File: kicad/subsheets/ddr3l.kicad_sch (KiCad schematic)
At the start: 1 part, among them U5 MT41K256M16TW-107:P

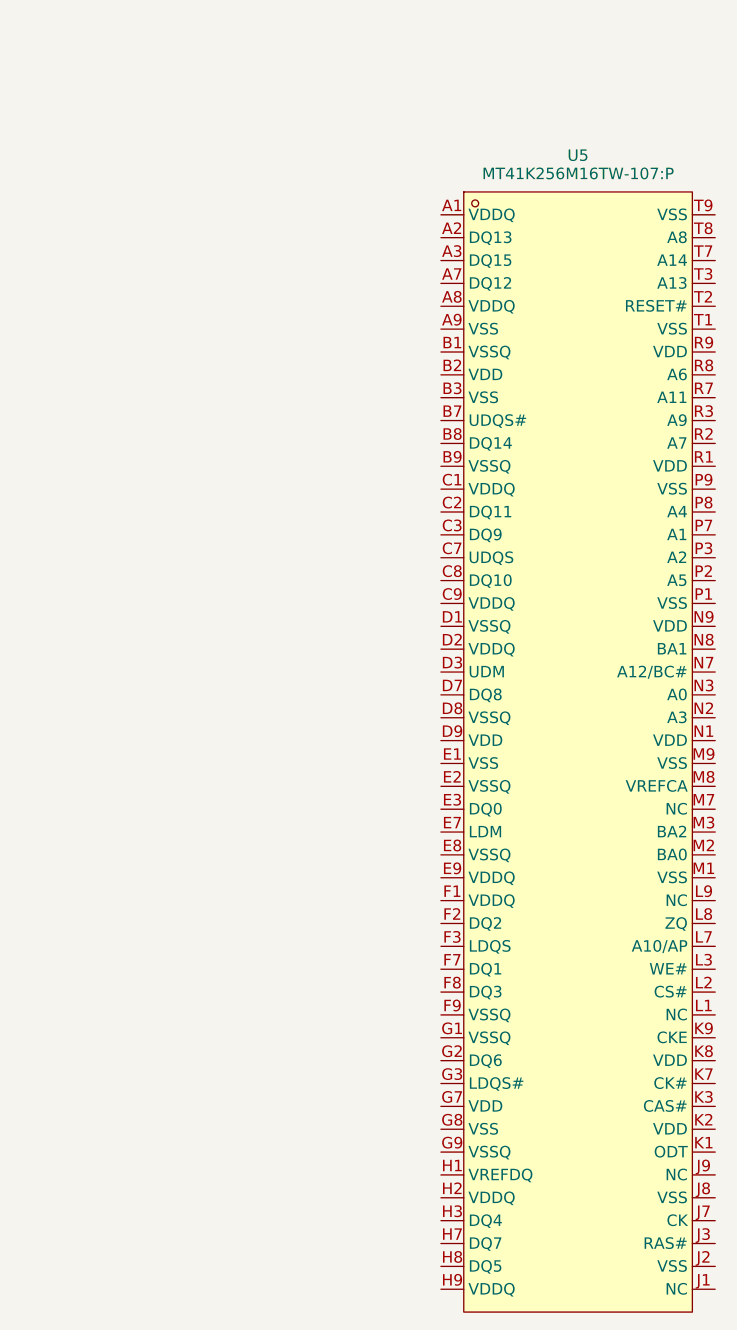
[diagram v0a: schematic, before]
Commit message: Resize sheets
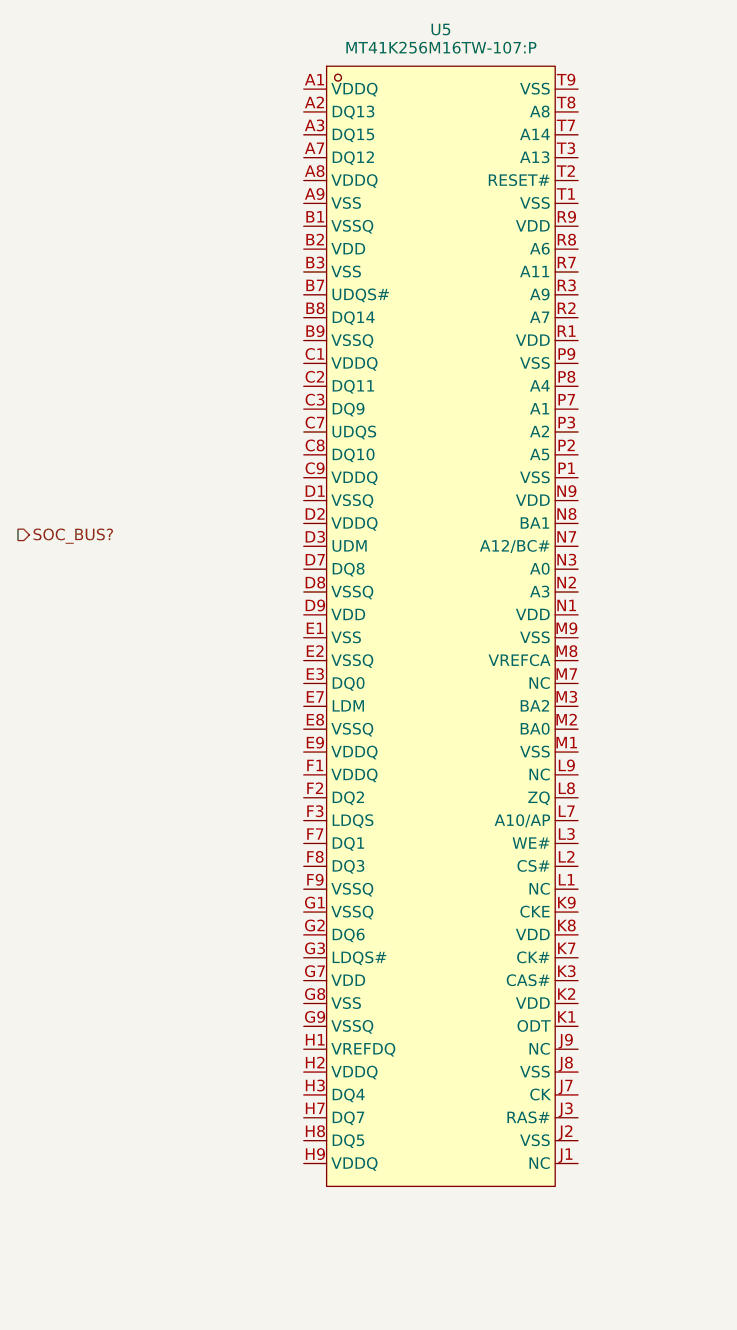
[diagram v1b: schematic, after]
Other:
- moved on the sheet: U5
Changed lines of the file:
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@@
 	(generator "eeschema")
 	(generator_version "9.0")
-	(paper "A4")
+	(paper "User" 140 190)
+	(hierarchical_label "SOC_BUS?"
+		(shape output)
+		(at 31.75 71.12 0)
+		(effects
+			(font
+				(size 1.27 1.27)
+			)
+			(justify left)
+		)
+	)
 	(symbol
 		(lib_id "srad-camera-symbols:MT41K256M16TW-107{colon}P")
-		(at 93.98 96.52 0)
+		(at 78.74 82.55 0)
 		(unit 1)
 		(exclude_from_sim no)
@@
 		(dnp no)
 		(property "Reference" "U5"
-			(at 93.98 29.718 0)
+			(at 78.74 15.748 0)
 			(effects
 				(font
@@
 		)
 		(property "Value" "MT41K256M16TW-107:P"
-			(at 93.98 31.75 0)
+			(at 78.74 17.78 0)
 			(effects
 				(font
@@
 		)
 		(property "Footprint" "FBGA-96_L14.0-W8.0-R16-C6-P0.80-TL"
-			(at 93.98 96.52 0)
+			(at 78.74 82.55 0)
 			(effects
 				(font
@@
 		)
 		(property "Datasheet" "https://atta.szlcsc.com/upload/public/pdf/source/20190702/C253882_073A45851B86D33155EFFA955E523761.pdf"
-			(at 93.98 96.52 0)
+			(at 78.74 82.55 0)
 			(effects
 				(font
@@
 		)
 		(property "Description" ""
-			(at 93.98 96.52 0)
+			(at 78.74 82.55 0)
 			(effects
 				(font
@@
 		)
 		(property "SYMBOL" "MT41K256M16TW-107:P"
-			(at 93.98 96.52 0)
+			(at 78.74 82.55 0)
 			(effects
 				(font
@@
 		)
 		(property "DEVICE" "MT41K256M16TW-107:P"
-			(at 93.98 96.52 0)
+			(at 78.74 82.55 0)
 			(effects
 				(font
@@
 		)
 		(property "LCSC PART NAME" "MT41K256M16TW-107:PTR"
-			(at 93.98 96.52 0)
+			(at 78.74 82.55 0)
 			(effects
 				(font
@@
 		)
 		(property "SUPPLIER PART" "C253882"
-			(at 93.98 96.52 0)
+			(at 78.74 82.55 0)
 			(effects
 				(font
@@
 		)
 		(property "MANUFACTURER" "micron(镁光)"
-			(at 93.98 96.52 0)
+			(at 78.74 82.55 0)
 			(effects
 				(font
@@
 		)
 		(property "MANUFACTURER PART" "MT41K256M16TW-107:P"
-			(at 93.98 96.52 0)
+			(at 78.74 82.55 0)
 			(effects
 				(font
@@
 		)
 		(property "SUPPLIER FOOTPRINT" "TFBGA-96"
-			(at 93.98 96.52 0)
+			(at 78.74 82.55 0)
 			(effects
 				(font
@@
 		)
 		(property "JLCPCB PART CLASS" "Extended Part"
-			(at 93.98 96.52 0)
+			(at 78.74 82.55 0)
 			(effects
 				(font
@@
 		)
 		(property "DATASHEET" "https://atta.szlcsc.com/upload/public/pdf/source/20190702/C253882_073A45851B86D33155EFFA955E523761.pdf"
-			(at 93.98 96.52 0)
+			(at 78.74 82.55 0)
 			(effects
 				(font
@@
 		)
 		(property "SUPPLIER" "LCSC"
-			(at 93.98 96.52 0)
+			(at 78.74 82.55 0)
 			(effects
 				(font
@@
 		)
 		(property "ADD INTO BOM" "yes"
-			(at 93.98 96.52 0)
+			(at 78.74 82.55 0)
 			(effects
 				(font
@@
 		)
 		(property "CONVERT TO PCB" "yes"
-			(at 93.98 96.52 0)
+			(at 78.74 82.55 0)
 			(effects
 				(font

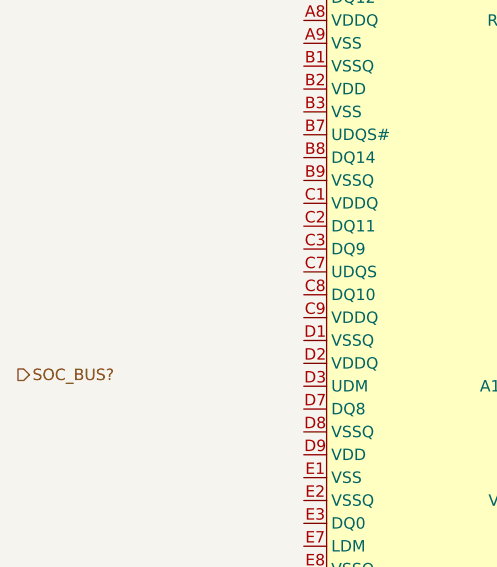
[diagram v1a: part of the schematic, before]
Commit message: Clean up root sheet, add power supply subsheet
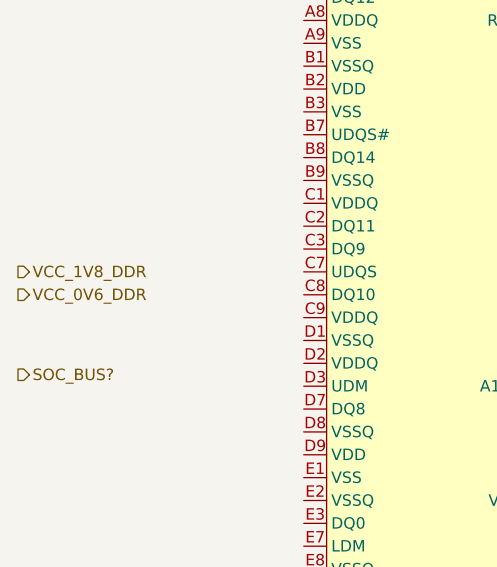
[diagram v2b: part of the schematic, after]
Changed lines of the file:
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@@
 	(generator_version "9.0")
 	(paper "User" 140 190)
+	(hierarchical_label "VCC_1V8_DDR"
+		(shape output)
+		(at 31.75 59.69 0)
+		(effects
+			(font
+				(size 1.27 1.27)
+			)
+			(justify left)
+		)
+	)
+	(hierarchical_label "VCC_0V6_DDR"
+		(shape output)
+		(at 31.75 62.23 0)
+		(effects
+			(font
+				(size 1.27 1.27)
+			)
+			(justify left)
+		)
+	)
 	(hierarchical_label "SOC_BUS?"
 		(shape output)

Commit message: Annotations
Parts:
- renumbered U5 to U6
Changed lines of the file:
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@@
 		(on_board yes)
 		(dnp no)
-		(property "Reference" "U5"
+		(property "Reference" "U6"
 			(at 78.74 15.748 0)
 			(effects
@@
 			(project "srad-camera"
 				(path "/da62c771-e8c9-451f-8df1-ec995aadcb11/51b69045-7733-4023-95b9-0aef3b91d808"
-					(reference "U5")
+					(reference "U6")
 					(unit 1)
 				)

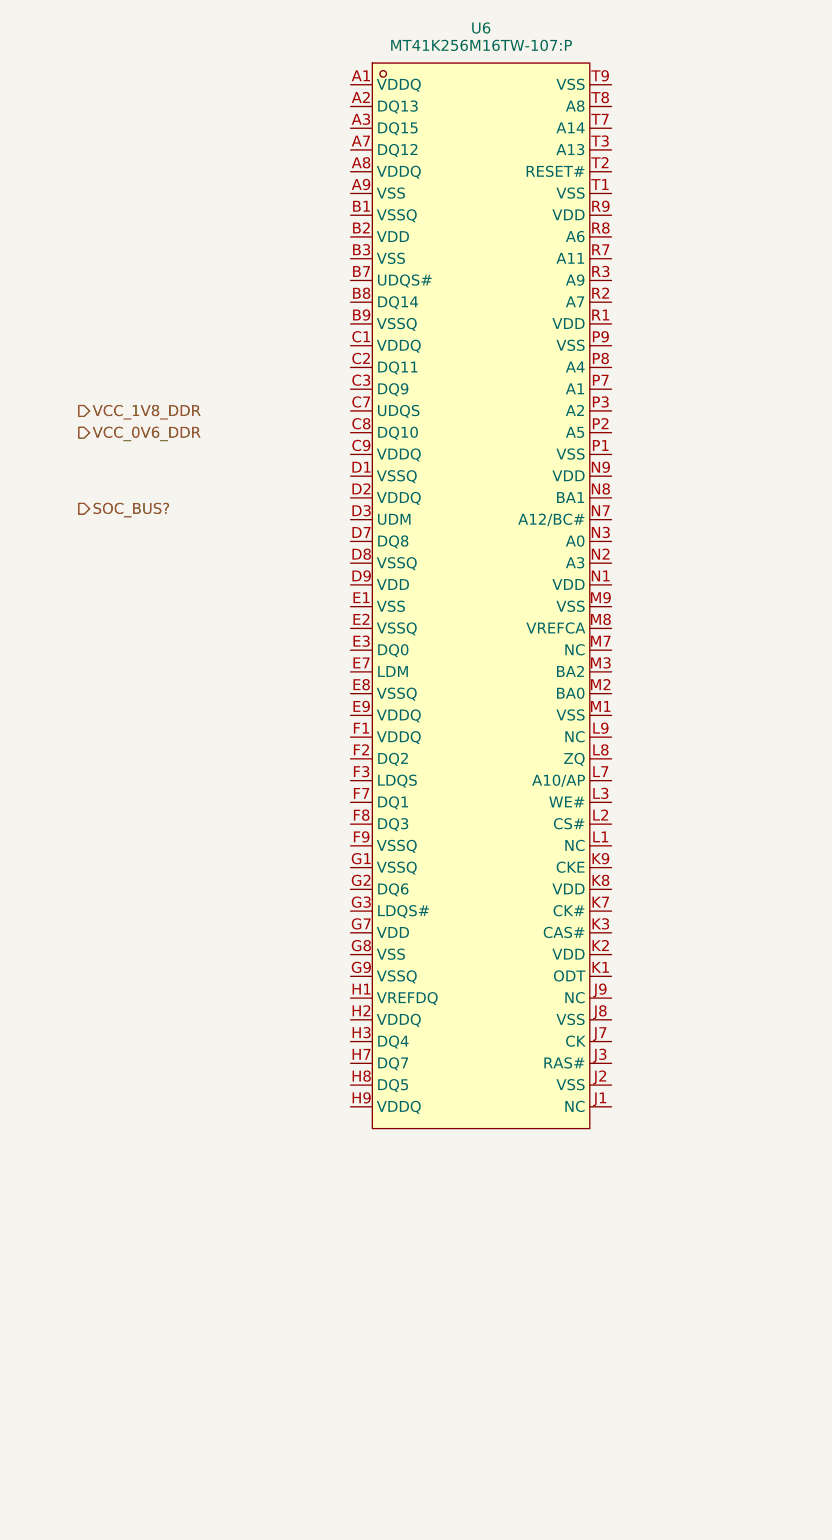
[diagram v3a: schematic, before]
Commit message: Wire up DDR3L
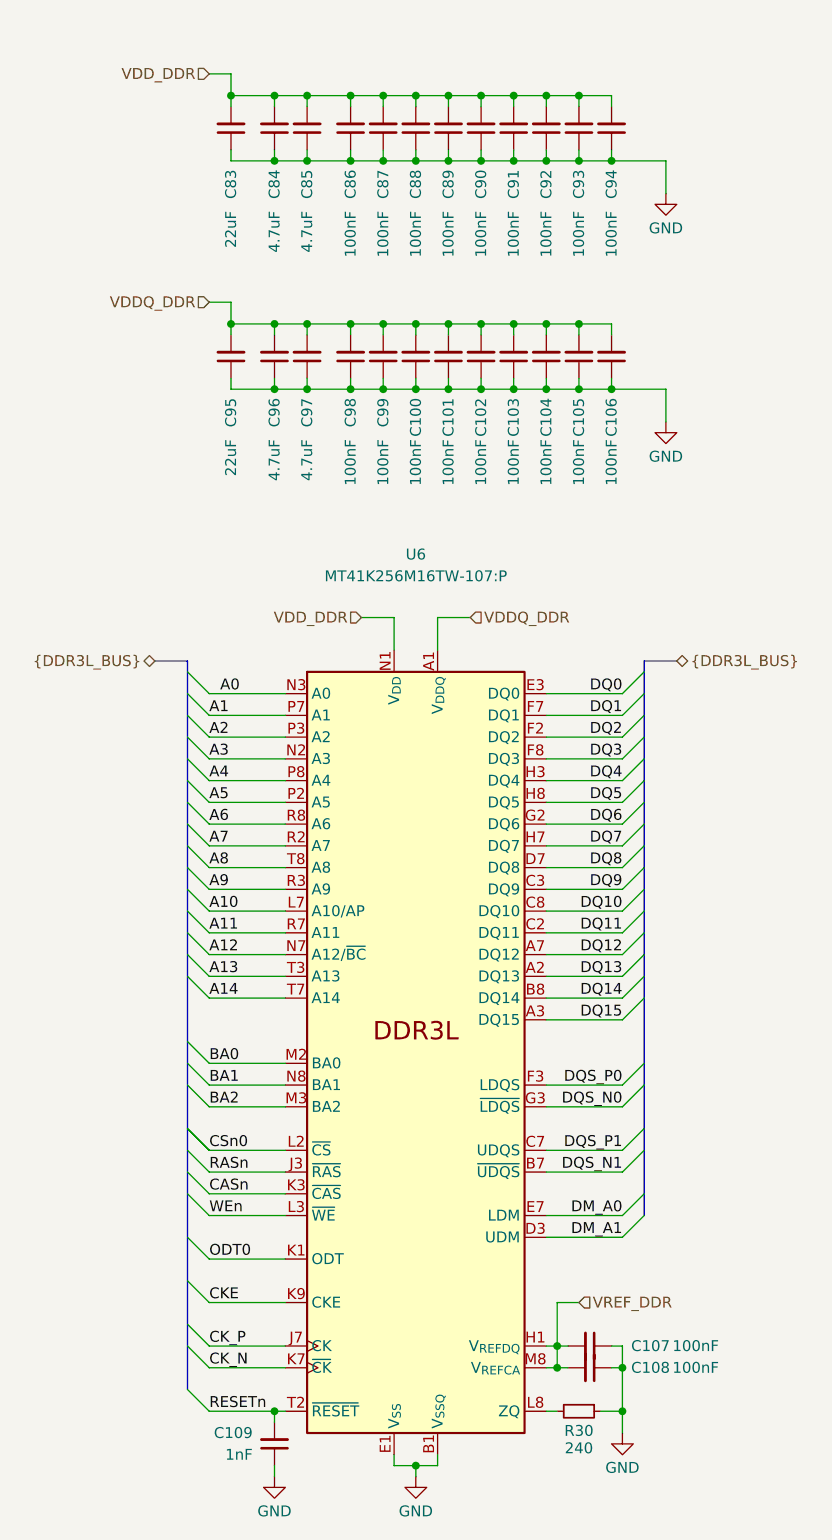
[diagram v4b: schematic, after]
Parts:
- removed U6: MT41K256M16TW-107:P, FBGA-96_L14.0-W8.0-R16-C6-P0.80-TL, symbol srad-camera-symbols:MT41K256M16TW-107{colon}P
- added C100, C101, C102, C103, C104, C105, C106, C107, C108, C86, C87, C88, C89, C90, C91, C92, C93, C94, C98, C99: 100nF, symbol Device:C_Small
- added C109: 1nF, symbol Device:C_Small
- added C83, C95: 22uF, symbol Device:C_Small
- added C84, C85, C96, C97: 4.7uF, symbol Device:C_Small
- added R30: 240, symbol Device:R_Small
- added U6: MT41K256M16TW-107:P, Package_BGA:Micron_FBGA-96_8x14mm_Layout9x16_P0.8mm, symbol Memory_RAM:MT41K256M16TW
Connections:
- new net: R30.2, U6.L8 (ZQ)
- new net A0: U6.N3 (A0)
- new net A1: U6.P7 (A1)
- new net A10: U6.L7 (A10/AP)
- new net A11: U6.R7 (A11)
- new net A12: U6.N7 (A12/~{BC})
- new net A13: U6.T3 (A13)
- new net A14: U6.T7 (A14)
- new net A2: U6.P3 (A2)
- new net A3: U6.N2 (A3)
- new net A4: U6.P8 (A4)
- new net A5: U6.P2 (A5)
- new net A6: U6.R8 (A6)
- new net A7: U6.R2 (A7)
- new net A8: U6.T8 (A8)
- new net A9: U6.R3 (A9)
- new net BA0: U6.M2 (BA0)
- new net BA1: U6.N8 (BA1)
- new net BA2: U6.M3 (BA2)
- new net CASn: U6.K3 (~{CAS})
- new net CKE: U6.K9 (CKE)
- new net CK_N: U6.K7 (~{CK})
- new net CK_P: U6.J7 (CK)
- new net CSn0: U6.L2 (~{CS})
- new net DM_A0: U6.E7 (LDM)
- new net DM_A1: U6.D3 (UDM)
- new net DQ0: U6.E3 (DQ0)
- new net DQ1: U6.F7 (DQ1)
- new net DQ10: U6.C8 (DQ10)
- new net DQ11: U6.C2 (DQ11)
- new net DQ12: U6.A7 (DQ12)
- new net DQ13: U6.A2 (DQ13)
- new net DQ14: U6.B8 (DQ14)
- new net DQ15: U6.A3 (DQ15)
- new net DQ2: U6.F2 (DQ2)
- new net DQ3: U6.F8 (DQ3)
- new net DQ4: U6.H3 (DQ4)
- new net DQ5: U6.H8 (DQ5)
- new net DQ6: U6.G2 (DQ6)
- new net DQ7: U6.H7 (DQ7)
- new net DQ8: U6.D7 (DQ8)
- new net DQ9: U6.C3 (DQ9)
- new net DQS_N0: U6.G3 (~{LDQS})
- new net DQS_N1: U6.B7 (~{UDQS})
- new net DQS_P0: U6.F3 (LDQS)
- new net DQS_P1: U6.C7 (UDQS)
- new net GND: C100.1, C101.1, C102.1, C103.1, C104.1, C105.1, C106.1, C107.1, C108.1, C109.1, C83.1, C84.1, C85.1, C86.1, C87.1, C88.1, C89.1, C90.1, C91.1, C92.1, C93.1, C94.1, C95.1, C96.1, C97.1, C98.1, C99.1, R30.1, U6.A9 (V_{SS}), U6.B1 (V_{SSQ}), U6.B3 (V_{SS}), U6.B9 (V_{SSQ}), U6.D1 (V_{SSQ}), U6.D8 (V_{SSQ}), U6.E1 (V_{SS}), U6.E2 (V_{SSQ}), U6.E8 (V_{SSQ}), U6.F9 (V_{SSQ}), U6.G1 (V_{SSQ}), U6.G8 (V_{SS}), U6.G9 (V_{SSQ}), U6.J2 (V_{SS}), U6.J8 (V_{SS}), U6.M1 (V_{SS}), U6.M9 (V_{SS}), U6.P1 (V_{SS}), U6.P9 (V_{SS}), U6.T1 (V_{SS}), U6.T9 (V_{SS})
- new net ODT0: U6.K1 (ODT)
- new net RASn: U6.J3 (~{RAS})
- new net RESETn: C109.2, U6.T2 (~{RESET})
- new net VDDQ_DDR: C100.2, C101.2, C102.2, C103.2, C104.2, C105.2, C106.2, C95.2, C96.2, C97.2, C98.2, C99.2, U6.A1 (V_{DDQ}), U6.A8 (V_{DDQ}), U6.C1 (V_{DDQ}), U6.C9 (V_{DDQ}), U6.D2 (V_{DDQ}), U6.E9 (V_{DDQ}), U6.F1 (V_{DDQ}), U6.H2 (V_{DDQ}), U6.H9 (V_{DDQ})
- new net VDD_DDR: C83.2, C84.2, C85.2, C86.2, C87.2, C88.2, C89.2, C90.2, C91.2, C92.2, C93.2, C94.2, U6.B2 (V_{DD}), U6.D9 (V_{DD}), U6.G7 (V_{DD}), U6.K2 (V_{DD}), U6.K8 (V_{DD}), U6.N1 (V_{DD}), U6.N9 (V_{DD}), U6.R1 (V_{DD}), U6.R9 (V_{DD})
- new net VREF_DDR: C107.2, C108.2, U6.H1 (V_{REFDQ}), U6.M8 (V_{REFCA})
- new net WEn: U6.L3 (~{WE})
